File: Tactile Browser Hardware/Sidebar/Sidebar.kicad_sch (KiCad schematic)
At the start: 38 parts, among them J1 Conn_01x02_Pin, J2 Conn_01x02_Pin, J3 Barrel_Jack_Switch, J4 Conn_01x02_Pin, SW10 SW_Push, SW11 SW_Push, SW12 SW_Push, SW6 SW_Push, SW7 SW_Push, SW8 SW_Push, SW9 SW_Push

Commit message: started sidebar pcb
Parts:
- AudioSpeed1, Volume1: footprint Rotary_Encoder:RotaryEncoder_Bourns_Horizontal_PEC12R-2x17F-Sxxxx -> Rotary_Encoder:RotaryEncoder_Alps_EC11E-Switch_Vertical_H20mm
- J2: footprint TerminalBlock_MetzConnect:TerminalBlock_MetzConnect_Type011_RT05503HBLC_1x03_P5.00mm_Horizontal -> TerminalBlock_Phoenix:ScrewTerminal_Vertical_1935310
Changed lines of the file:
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@@
 			)
 		)
-		(property "Footprint" "Rotary_Encoder:RotaryEncoder_Bourns_Horizontal_PEC12R-2x17F-Sxxxx"
+		(property "Footprint" "Rotary_Encoder:RotaryEncoder_Alps_EC11E-Switch_Vertical_H20mm"
 			(at 184.15 20.066 0)
 			(effects
@@
 			)
 		)
-		(property "Footprint" "TerminalBlock_MetzConnect:TerminalBlock_MetzConnect_Type011_RT05503HBLC_1x03_P5.00mm_Horizontal"
+		(property "Footprint" "TerminalBlock_Phoenix:ScrewTerminal_Vertical_1935310"
 			(at 119.38 31.75 0)
 			(effects
@@
 			)
 		)
-		(property "Footprint" "Rotary_Encoder:RotaryEncoder_Bourns_Horizontal_PEC12R-2x17F-Sxxxx"
+		(property "Footprint" "Rotary_Encoder:RotaryEncoder_Alps_EC11E-Switch_Vertical_H20mm"
 			(at 220.98 21.336 0)
 			(effects

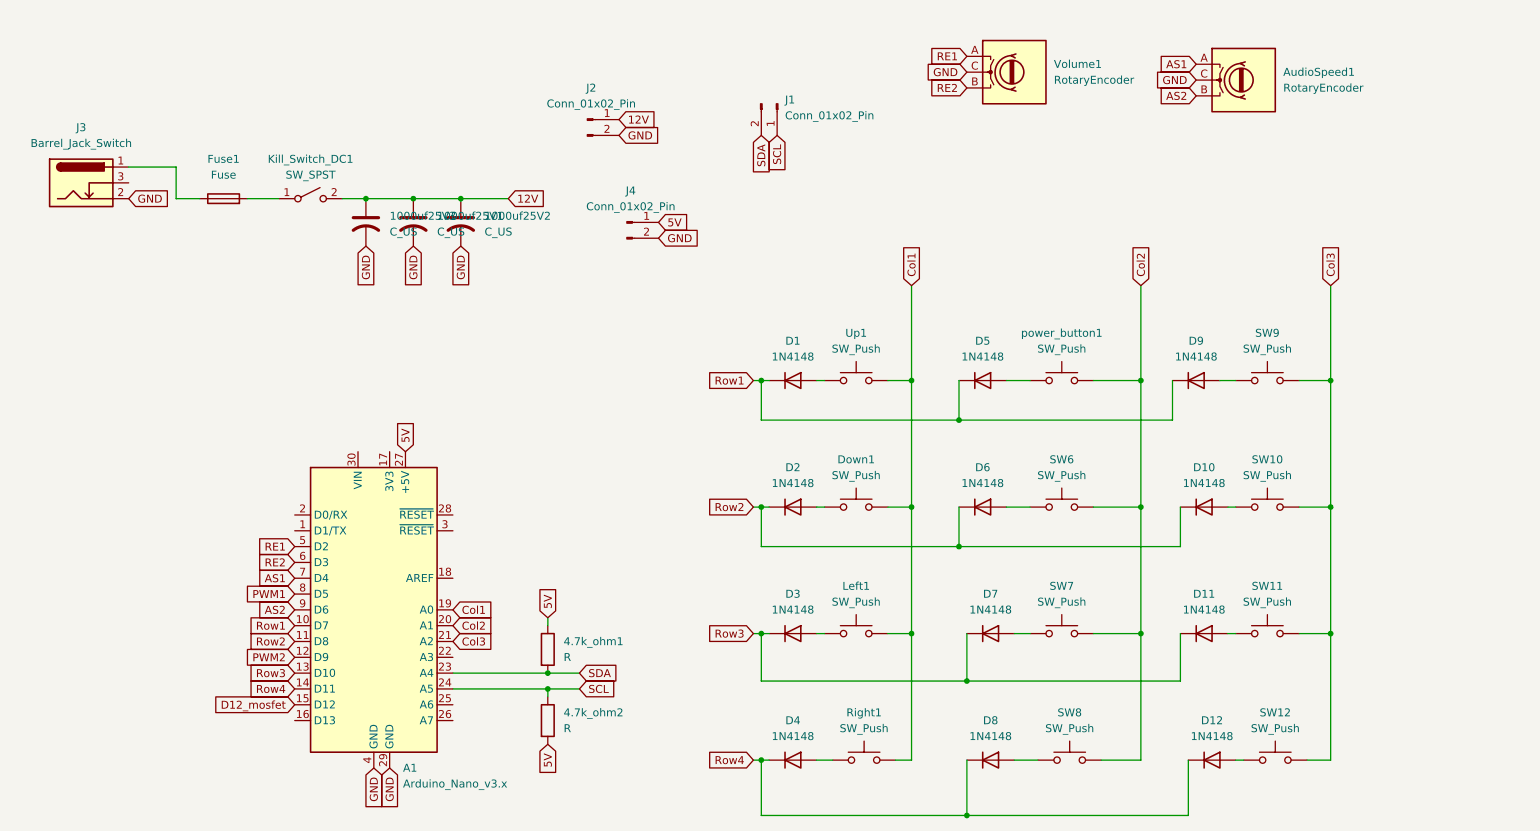
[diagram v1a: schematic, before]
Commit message: added power mosfet
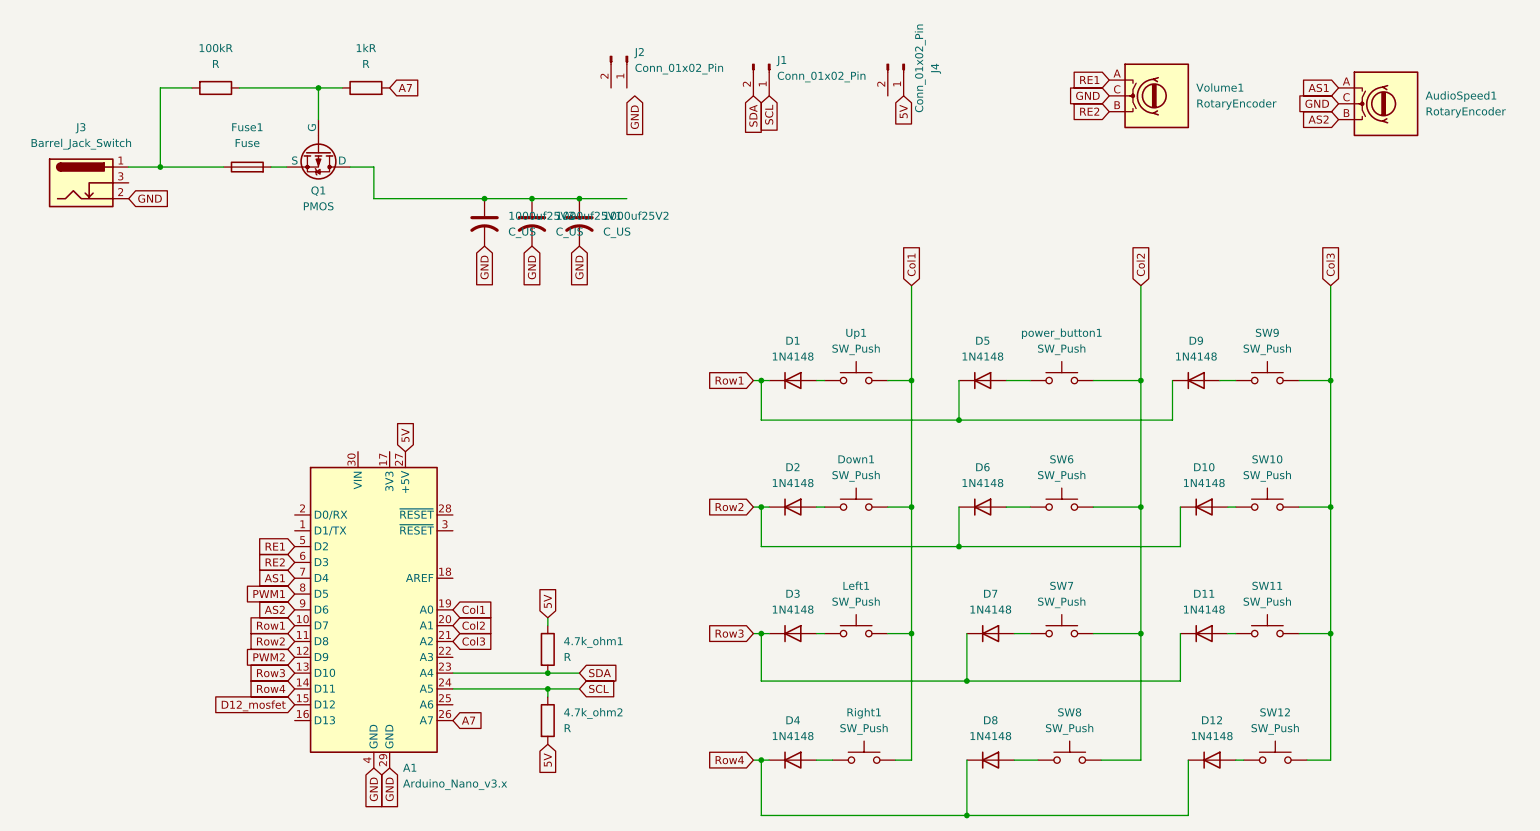
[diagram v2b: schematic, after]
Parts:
- removed Kill_Switch_DC1: SW_SPST, Button_Switch_Keyboard:SW_Cherry_MX_1.00u_PCB, symbol Switch:SW_SPST
- added 100kR, 1kR: R, symbol Device:R
- added Q1: PMOS, symbol Simulation_SPICE:PMOS
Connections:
- net GND: no longer J2.2 (Pin_2), J4.2 (Pin_2)
- net A7: now reaches A1.26 (A7)
- net A7: now also 1kR.2
- net at Fuse1.1, J3.1: now also 100kR.2
- net at Fuse1.2: now also Q1.3 (S)
- net 12V: no longer names the net of 1000uf25V1.1, 1000uf25V2.1, 1000uf25V3.1
- net 12V: now also Q1.1 (D); no longer J2.1 (Pin_1)
- new net: 100kR.1, 1kR.1, Q1.2 (G)
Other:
- moved on the sheet: 1000uf25V1, 1000uf25V2, 1000uf25V3, AudioSpeed1, Fuse1, J1, J2, J4, Volume1

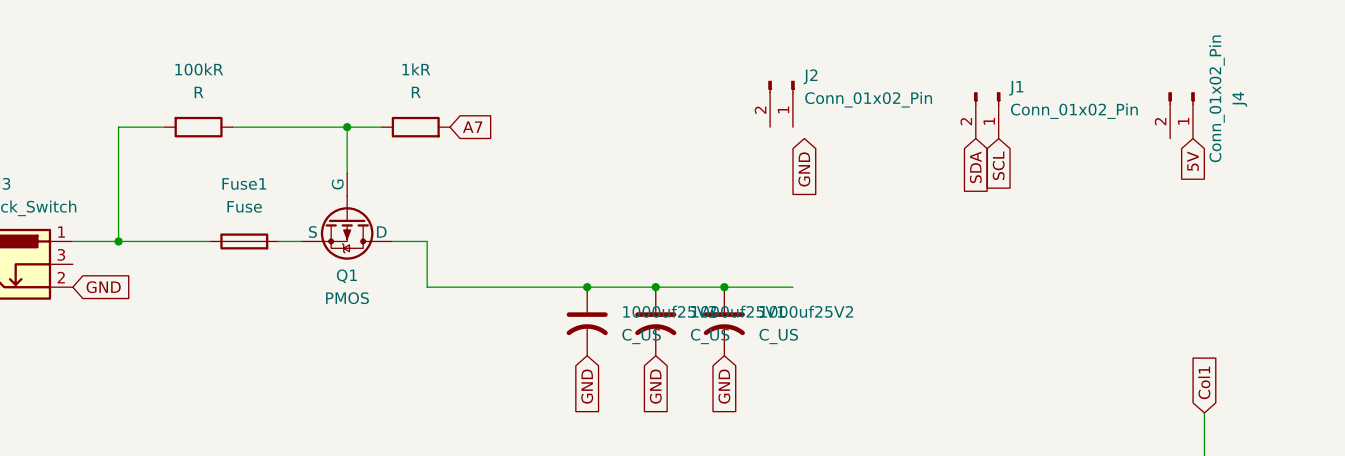
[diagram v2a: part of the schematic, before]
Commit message: correct mosfet footprints
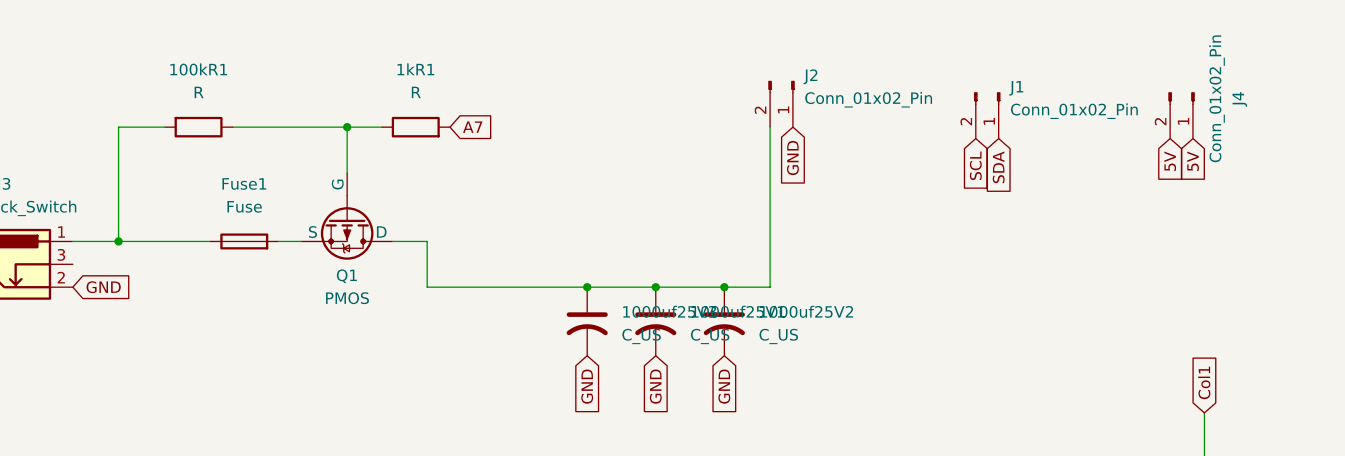
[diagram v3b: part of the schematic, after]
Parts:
- 100kR1: renamed from 100kR; footprint (none) -> Resistor_SMD:R_0805_2012Metric
- 1kR1: renamed from 1kR; footprint (none) -> Resistor_SMD:R_0805_2012Metric
- Q1: footprint (none) -> Package_TO_SOT_SMD:TO-252-3_TabPin2
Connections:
- net 5V: now also J4.2 (Pin_2)
- net GND: now also J2.1 (Pin_1)
- net SCL: now also J1.2 (Pin_2); no longer J1.1 (Pin_1)
- net SDA: now also J1.1 (Pin_1); no longer J1.2 (Pin_2)
- net at J2.2 (Pin_2): now also 1000uf25V1.1, 1000uf25V2.1, 1000uf25V3.1, Q1.1 (D)
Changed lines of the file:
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@@
 	)
 	(junction
-		(at 118.11 44.45)
-		(diameter 0)
-		(color 0 0 0 0)
-	)
-	(junction
 		(at 238.76 93.98)
 		(diameter 0)
@@
 	)
 	(junction
+		(at 118.11 44.45)
+		(diameter 0)
+		(color 0 0 0 0)
+	)
+	(junction
 		(at 102.87 44.45)
 		(diameter 0)
@@
 	(wire
 		(pts
+			(xy 118.11 44.45) (xy 123.19 44.45)
+		)
+		(stroke
+			(width 0)
+			(type default)
+		)
+	)
+	(wire
+		(pts
 			(xy 233.68 73.66) (xy 238.76 73.66)
 		)
@@
 	(wire
 		(pts
-			(xy 118.11 44.45) (xy 125.73 44.45)
-		)
-		(stroke
-			(width 0)
-			(type default)
-		)
-	)
-	(wire
-		(pts
 			(xy 208.28 58.42) (xy 208.28 73.66)
 		)
@@
 	(wire
 		(pts
+			(xy 123.19 44.45) (xy 123.19 26.67)
+		)
+		(stroke
+			(width 0)
+			(type default)
+		)
+	)
+	(wire
+		(pts
 			(xy 81.28 39.37) (xy 85.09 39.37)
 		)
@@
 	(global_label "GND"
 		(shape input)
-		(at 127 27.94 270)
+		(at 125.73 26.67 270)
 		(fields_autoplaced yes)
 		(effects
@@
 		)
 		(property "Intersheetrefs" "${INTERSHEET_REFS}"
-			(at 127 34.7957 90)
+			(at 125.73 33.5257 90)
 			(effects
 				(font
@@
 		)
 	)
+	(global_label "5V"
+		(shape input)
+		(at 167.64 27.94 270)
+		(fields_autoplaced yes)
+		(effects
+			(font
+				(size 1.27 1.27)
+			)
+			(justify right)
+		)
+		(property "Intersheetrefs" "${INTERSHEET_REFS}"
+			(at 167.64 33.2233 90)
+			(effects
+				(font
+					(size 1.27 1.27)
+				)
+				(justify right)
+				(hide yes)
+			)
+		)
+	)
 	(global_label "AS2"
 		(shape input)
@@
 	(global_label "SDA"
 		(shape input)
-		(at 146.05 27.94 270)
+		(at 148.59 27.94 270)
 		(fields_autoplaced yes)
 		(effects
@@
 		)
 		(property "Intersheetrefs" "${INTERSHEET_REFS}"
-			(at 146.05 34.4933 90)
+			(at 148.59 34.4933 90)
 			(effects
 				(font
@@
 	(global_label "SCL"
 		(shape input)
-		(at 148.59 27.94 270)
+		(at 146.05 27.94 270)
 		(fields_autoplaced yes)
 		(effects
@@
 		)
 		(property "Intersheetrefs" "${INTERSHEET_REFS}"
-			(at 148.59 34.4328 90)
+			(at 146.05 34.4328 90)
 			(effects
 				(font
@@
 		(dnp no)
 		(fields_autoplaced yes)
-		(property "Reference" "1kR"
+		(property "Reference" "1kR1"
 			(at 83.82 20.32 90)
 			(effects
@@
 			)
 		)
-		(property "Footprint" ""
+		(property "Footprint" "Resistor_SMD:R_0805_2012Metric"
 			(at 83.82 28.448 90)
 			(effects
@@
 			(project ""
 				(path "/16cfaf40-0992-40a8-a734-5ca99128006a"
-					(reference "1kR")
+					(reference "1kR1")
 					(unit 1)
 				)
@@
 			)
 		)
-		(property "Footprint" ""
+		(property "Footprint" "Package_TO_SOT_SMD:TO-252-3_TabPin2"
 			(at 78.74 41.91 0)
 			(effects
@@
 		(dnp no)
 		(fields_autoplaced yes)
-		(property "Reference" "100kR"
+		(property "Reference" "100kR1"
 			(at 59.69 20.32 90)
 			(effects
@@
 			)
 		)
-		(property "Footprint" ""
+		(property "Footprint" "Resistor_SMD:R_0805_2012Metric"
 			(at 59.69 24.892 90)
 			(effects
@@
 			(project ""
 				(path "/16cfaf40-0992-40a8-a734-5ca99128006a"
-					(reference "100kR")
+					(reference "100kR1")
 					(unit 1)
 				)

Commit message: finally got the right fuse
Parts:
- Fuse1: footprint Fuse:Fuse_0402_1005Metric_Pad0.77x0.64mm_HandSolder -> fuse_3560:FUSE_3560
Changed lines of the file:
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@@
 			)
 		)
-		(property "Footprint" "Fuse:Fuse_0402_1005Metric_Pad0.77x0.64mm_HandSolder"
+		(property "Footprint" "fuse_3560:FUSE_3560"
 			(at 64.77 41.148 90)
 			(effects

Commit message: done with pcb connections
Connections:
- net D12_mosfet: now also 1kR1.2
- net A7: no longer names the net of A1.26 (A7)
- net A7: no longer 1kR1.2
